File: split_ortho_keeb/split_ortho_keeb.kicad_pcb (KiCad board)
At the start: 2 copper layers, 174 parts, among them J1 CONN_LCD, J2 TC2050-IDC, J3 USB_C_Receptacle_USB2.0, SW1 SW_Push, SW10 SW_Push, SW11 SW_Push, SW12 SW_Push, SW13 SW_Push, SW14 SW_Push, SW15 SW_Push, SW16 SW_Push, SW17 SW_Push, SW18 SW_Push, SW19 SW_Push, SW2 SW_Push, SW20 SW_Push, SW21 SW_Push, SW22 SW_Push, SW23 SW_Push, SW24 SW_Push, SW25 SW_Push, SW26 SW_Push, SW27 SW_Push, SW28 SW_Push, SW29 SW_Push, SW3 SW_Push, SW30 SW_Push, SW31 SW_Push, SW32 SW_Push, SW33 SW_Push, SW34 SW_Push, SW35 SW_Push, SW36 SW_Push, SW37 SW_Push, SW38 SW_Push, SW39 SW_Push, SW4 SW_Push, SW40 SW_Push, SW41 SW_Push, SW42 SW_Push, SW43 SW_Push, SW44 SW_Push, SW45 SW_Push, SW46 SW_Push, SW47 SW_Push, SW48 SW_Push, SW49 SW_Push, SW5 SW_Push, SW50 SW_Push, SW51 SW_Push, SW52 SW_Push, SW53 SW_Push, SW54 SW_Push, SW55 SW_Push, SW56 SW_Push, SW57 SW_Push, SW58 SW_Push, SW59 SW_Push, SW6 SW_Push, SW60 SW_Push, SW61 SW_Push, SW62 SW_Push, SW63 SW_Push, SW64 SW_Push, SW65 SW_Push, SW66 SW_Push, SW67 SW_Push, SW68 SW_Push, SW69 SW_Push, SW7 SW_Push, SW70 SW_Push, SW8 SW_Push, SW9 SW_Push, U1 STM32F303RCTx, U2 USBLC6-2SC6, U3 XC6206P332MR, Y1 32MHz

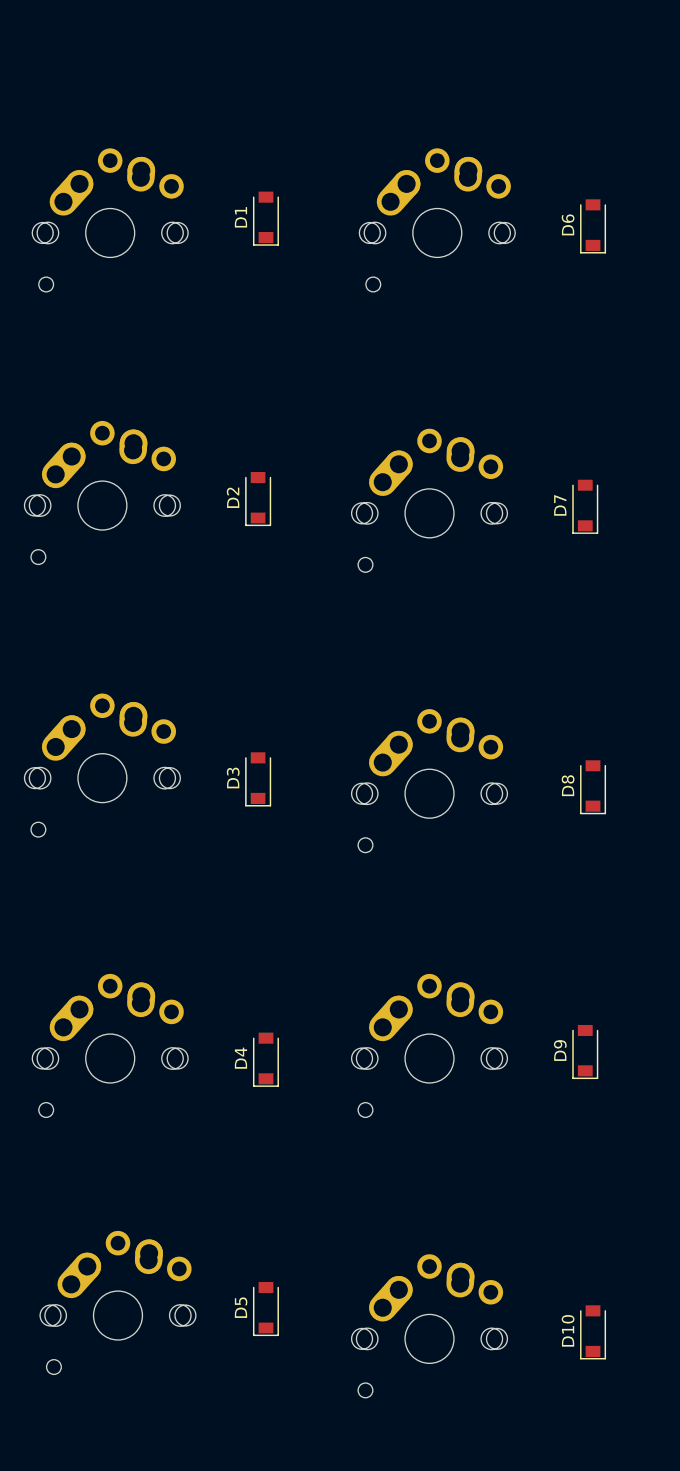
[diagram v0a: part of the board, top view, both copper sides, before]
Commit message: fixed some button placements
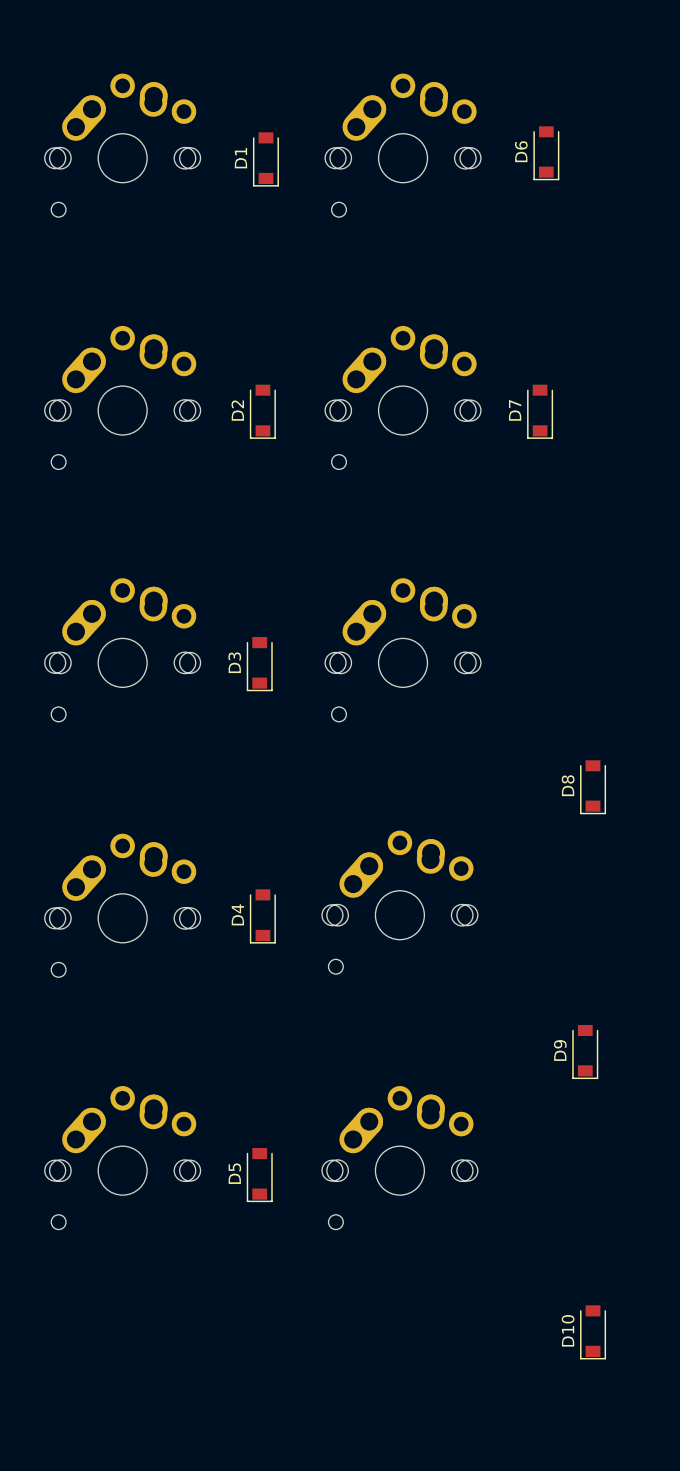
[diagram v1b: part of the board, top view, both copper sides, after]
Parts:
- moved SW10 13.9 mm to (75.7, 133.6)
- moved SW9 11.9 mm to (75.7, 112.8)
- moved SW5 11.8 mm to (53.1, 133.6)
- moved D4 11.7 mm to (64.5, 112.8)
- moved SW4 11.5 mm to (53.1, 113.0)
- moved D5 10.9 mm to (64.3, 133.9)
- moved SW8 10.9 mm to (75.9, 92.2)
- moved SW3 9.54 mm to (53.1, 92.2)
- moved D3 9.40 mm to (64.3, 92.2)
- moved SW7 8.66 mm to (75.9, 71.6)
- moved D7 8.58 mm to (87.1, 71.6)
- moved SW2 7.92 mm to (53.1, 71.6)
- moved D2 7.12 mm to (64.5, 71.6)
- moved D6 7.08 mm to (87.6, 50.5)
- moved SW6 6.71 mm to (75.9, 51.1)
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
